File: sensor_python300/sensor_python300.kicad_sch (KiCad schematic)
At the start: 68 parts, among them J101 DF40HC(4.0)-60DS-0.4V(51), U101 NOIP1SN0300A-QTI, U102 TPS22918DBVR, U103 TPS22918DBVR, U104 TPS22918DBVR, U105 APX803S, X101 <DNP> DSC1103DI5-360.0000

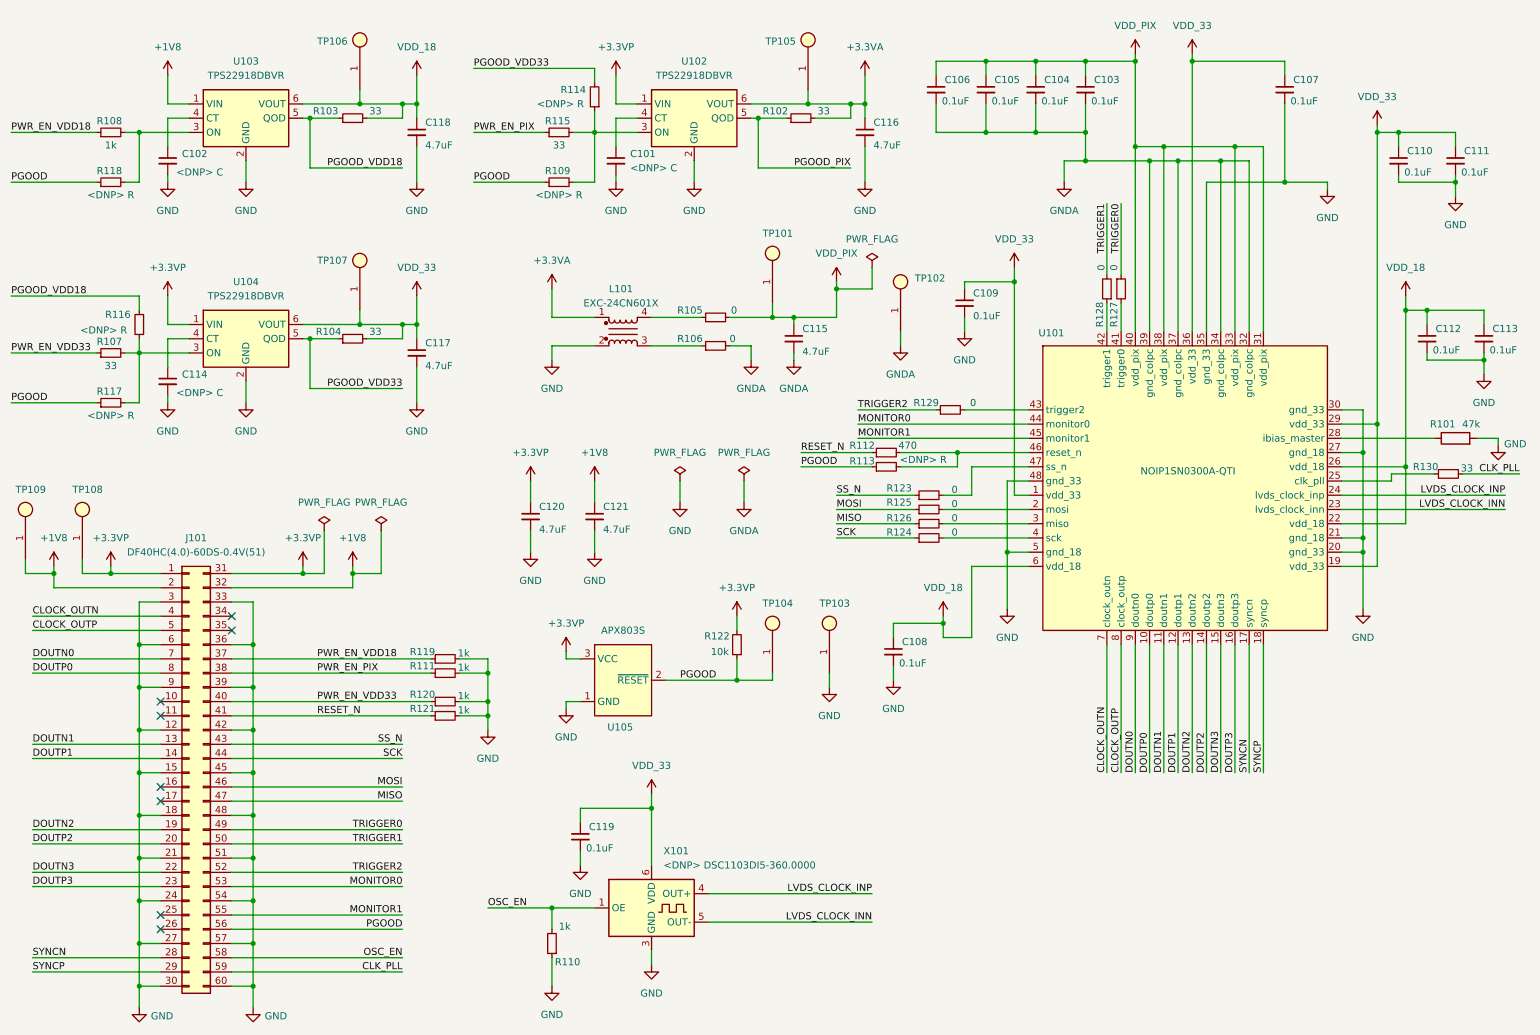
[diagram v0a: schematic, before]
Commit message: 電源回路を昇圧DC-DCを使うものに変更
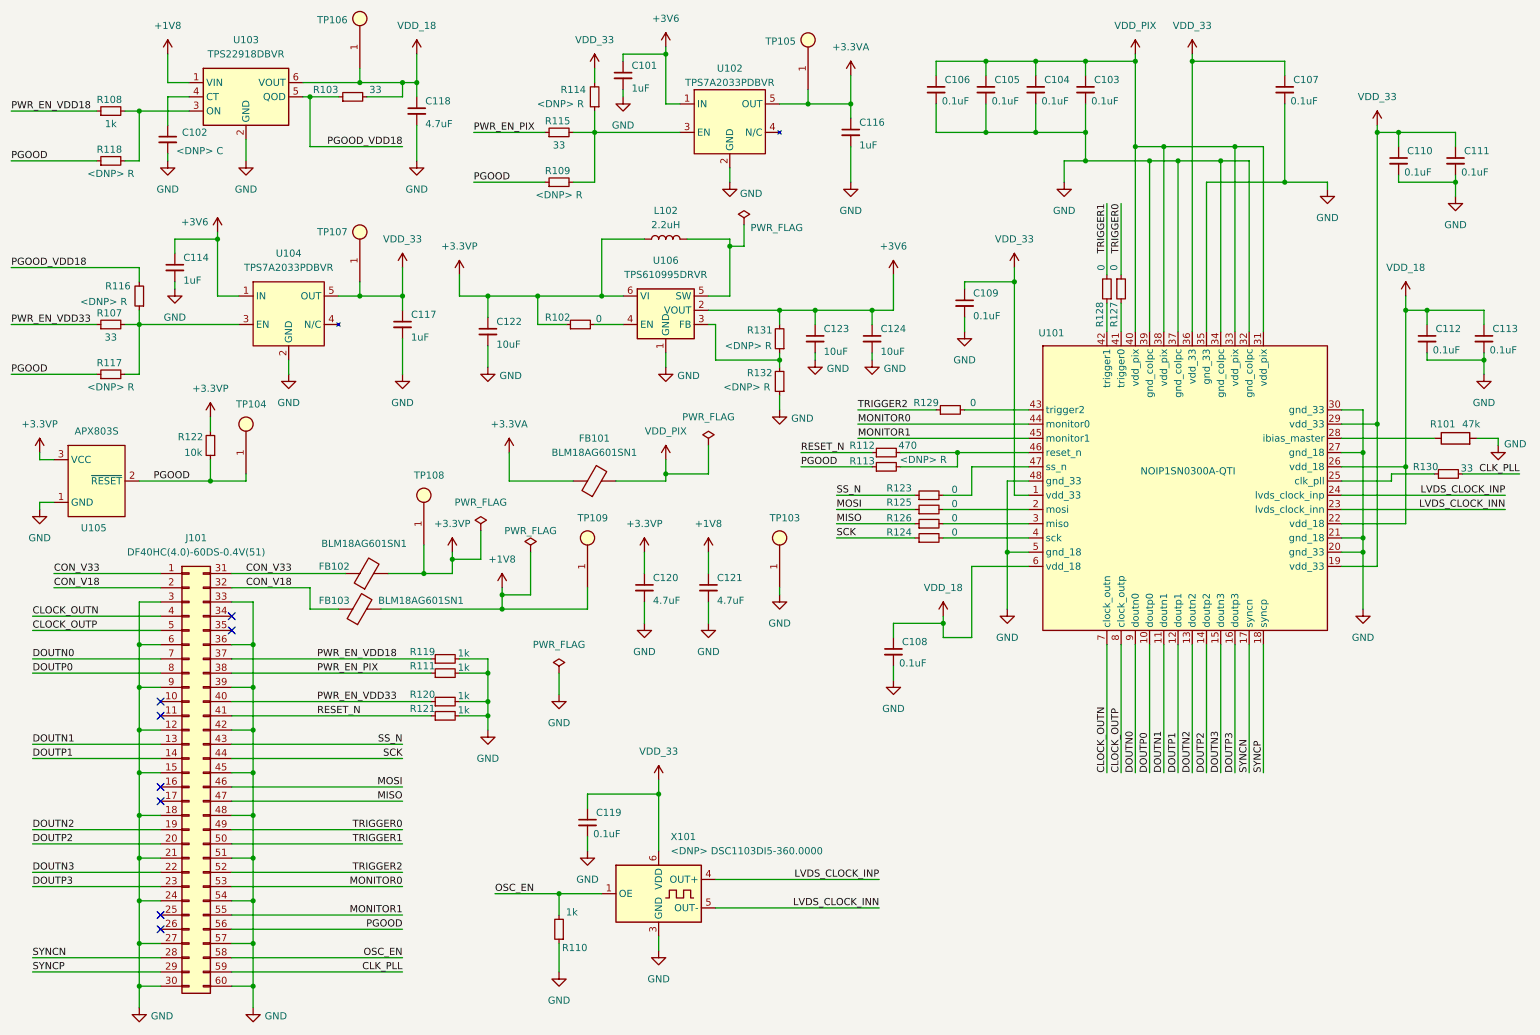
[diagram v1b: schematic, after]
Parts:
- removed C115: 4.7uF, Capacitor_SMD:C_0402_1005Metric, symbol Device:C_Small
- removed L101: EXC-24CN601X, sensor_python300:XMER_EXC-24CN601X_PAN, symbol Device:L_Iron_Coupled_1423
- removed R104: 33, Resistor_SMD:R_0402_1005Metric, symbol Device:R_Small
- removed R105, R106: 0, Resistor_SMD:R_0402_1005Metric, symbol Device:R_Small
- removed TP101, TP102: ~, sensor_python300:TestPin, symbol sensor_python300:TestPin
- removed U102, U104: TPS22918DBVR, Package_TO_SOT_SMD:SOT-23-6, symbol Power_Management:TPS22917DBV
- added C122, C123, C124: 10uF, Capacitor_SMD:C_0603_1608Metric, symbol Device:C_Small
- added FB101, FB102, FB103: BLM18AG601SN1, Inductor_SMD:L_0603_1608Metric, symbol Device:FerriteBead
- added L102: 2.2uH, Inductor_SMD:L_1008_2520Metric, symbol Device:L
- added R131, R132: <DNP> R, Resistor_SMD:R_0402_1005Metric, symbol Device:R_Small
- added U102, U104: TPS7A2033PDBVR, Package_TO_SOT_SMD:SOT-23-5, symbol sensor_python300:TPS7A2033PDBVR
- added U106: TPS610995DRVR, Package_SON:WSON-6-1EP_2x2mm_P0.65mm_EP1x1.6mm, symbol Regulator_Switching:TPS61099DRV
- C101, C114: value <DNP> C -> 1uF
- C116, C117: value 4.7uF -> 1uF
- R102: value 33 -> 0
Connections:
- net GNDA is gone; now on net GND: C103.2, C104.2, C105.2, C106.2, U101.32 (gnd_colpc), U101.34 (gnd_colpc), U101.37 (gnd_colpc), U101.39 (gnd_colpc)
- net PGOOD_PIX is gone; now on net +3.3VP: R102.1
- net PGOOD_VDD33 is gone; now on net VDD_33: R114.2
- net +1V8: now also FB103.2; no longer J101.2 (Pin_2), J101.32 (Pin_32)
- net +3.3VA: now also FB101.1, U102.5 (OUT); no longer R102.2
- net +3.3VP: now also C122.1, FB102.2, L102.1, U106.6 (VI); no longer J101.1 (Pin_1), J101.31 (Pin_31)
- net GND: now also C122.2, C123.2, C124.2, R132.1, U102.2 (GND), U104.2 (GND), U106.1 (GND), U106.7 (GND)
- net VDD_33: now also U104.5 (OUT)
- net VDD_PIX: now also FB101.2
- net at R107.2, R116.1, R117.2: now also U104.3 (EN)
- net at R109.2, R114.1, R115.2: now also U102.3 (EN)
- net +3V6: now reaches C101.1
- net +3V6: now also C114.1, C123.1, C124.1, R131.2, U102.1 (IN), U104.1 (IN), U106.2 (VOUT)
- new net: R102.2, U106.4 (EN)
- new net: R131.1, R132.2, U106.3 (FB)
- new net: L102.2, U106.5 (SW)
- new net CON_V18: FB103.1, J101.2 (Pin_2), J101.32 (Pin_32)
- new net CON_V33: FB102.1, J101.1 (Pin_1), J101.31 (Pin_31)
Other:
- moved on the sheet: C102, C116, C117, C118, C119, C120, C121, R103, R107, R108, R110, R116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
